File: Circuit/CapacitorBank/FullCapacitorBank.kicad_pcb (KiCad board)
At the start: 2 copper layers, 142.2 x 101.6 mm, 48 parts, among them J1 AC Power In, J2 Output+, J3 Output-, J4 To Voltage Sensing, Q1 BT138-800, Q2 BT138-800, SW1 SW_Push, T1 6:75+75, U1 PC817, U2 PC817

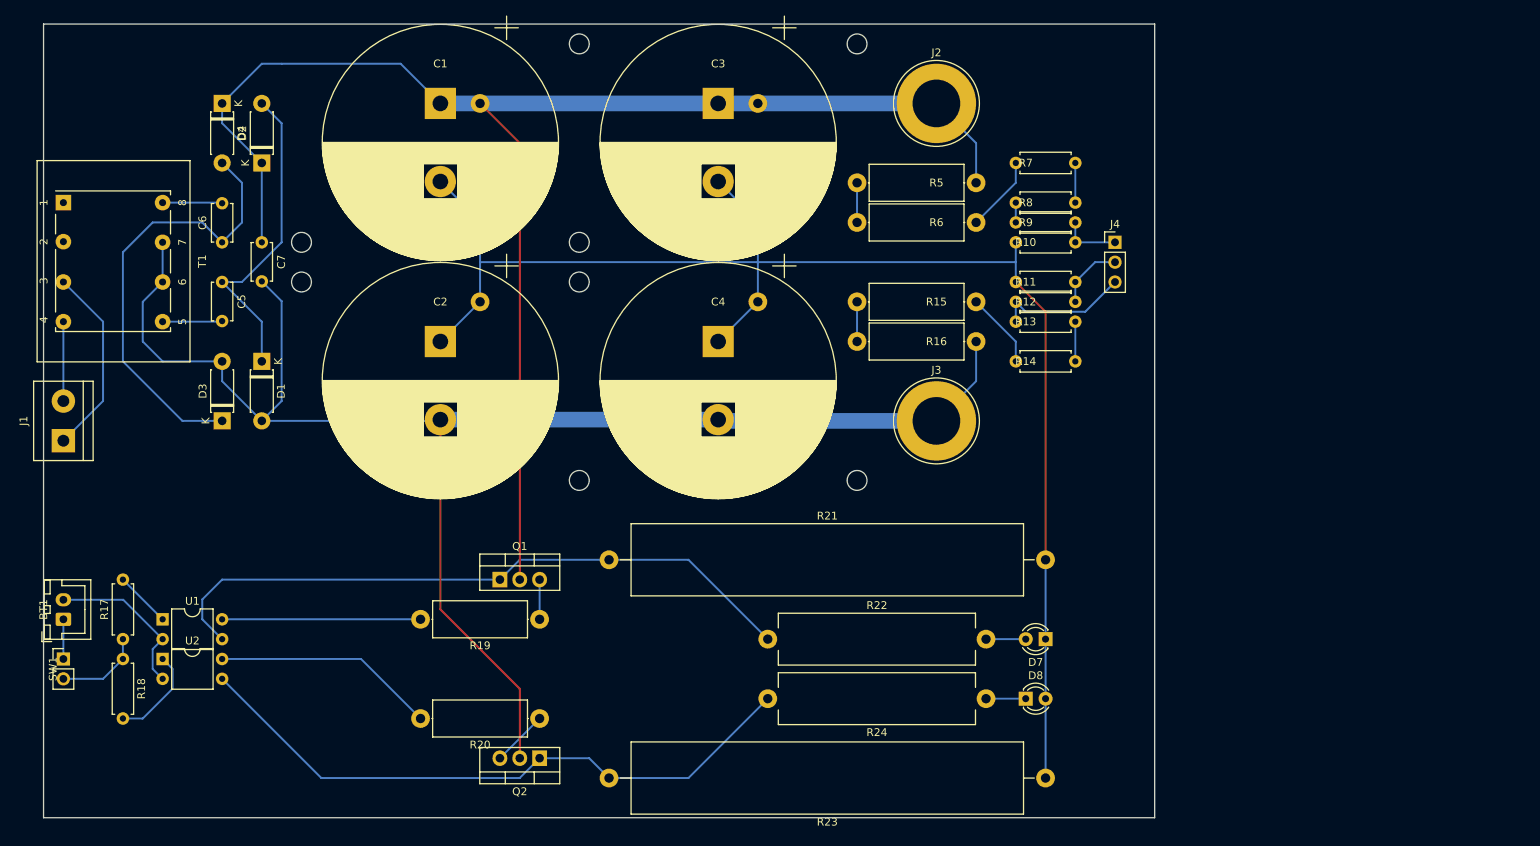
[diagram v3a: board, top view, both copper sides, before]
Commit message: [Circuit] Adjust footprint of customized components and optimize the PCB design
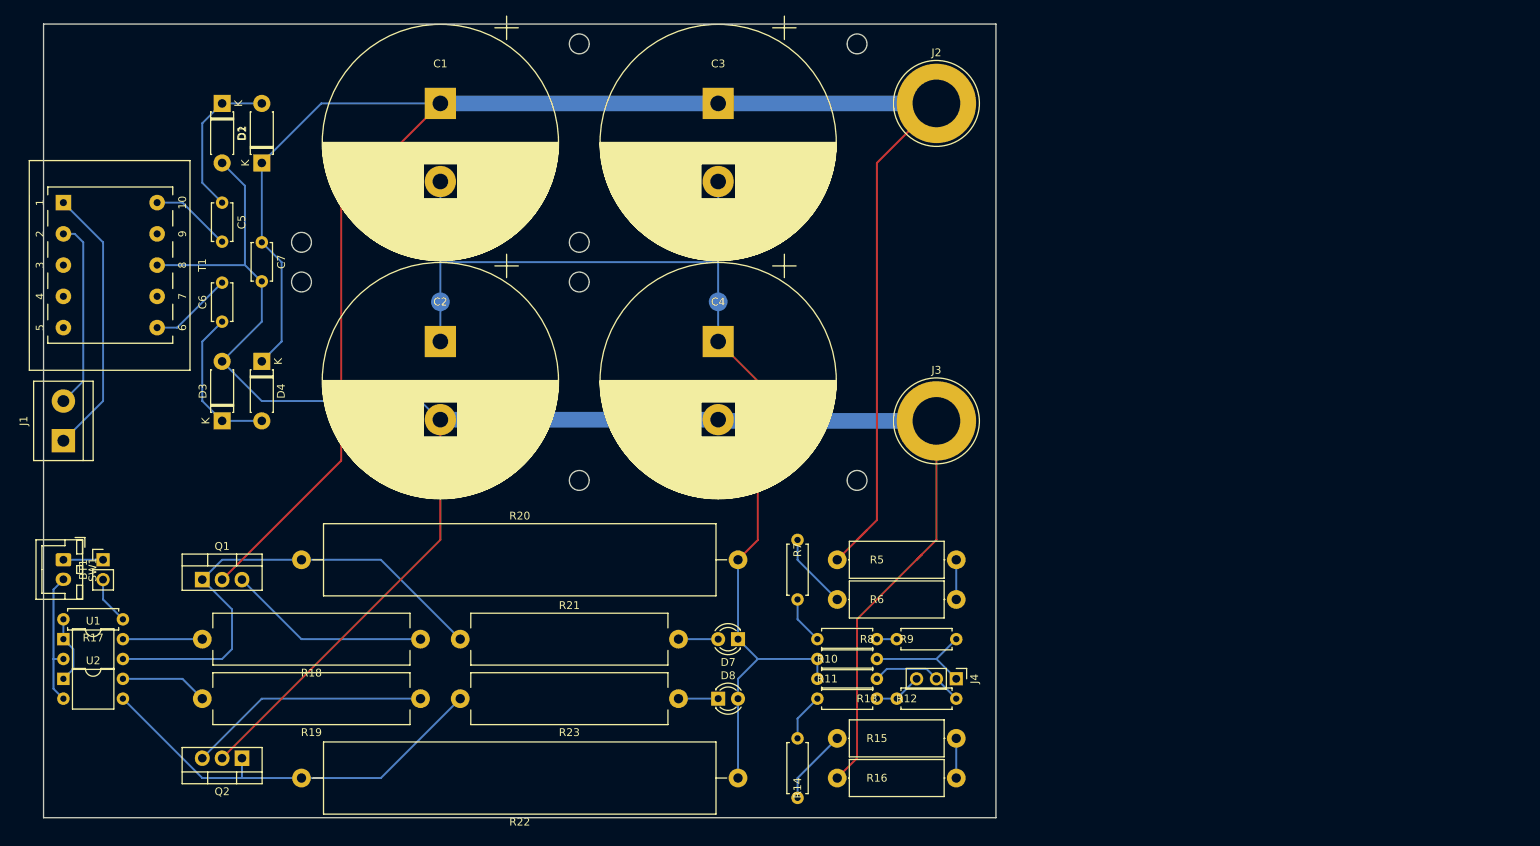
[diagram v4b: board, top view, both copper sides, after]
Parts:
- removed the R18 at (55.9, 114.3)
- R17: value 1K -> 510
- R18: renamed from R19; value 1M/1W -> 43K/5W; footprint Resistor_THT:R_Axial_DIN0414_L11.9mm_D4.5mm_P15.24mm_Horizontal -> Resistor_THT:R_Axial_Power_L25.0mm_W6.4mm_P27.94mm
- R19: renamed from R20; value 1M/1W -> 43K/5W; footprint Resistor_THT:R_Axial_DIN0414_L11.9mm_D4.5mm_P15.24mm_Horizontal -> Resistor_THT:R_Axial_Power_L25.0mm_W6.4mm_P27.94mm
- T1: footprint Power:Transformer_Generic_EE25_8Pin -> Power:Transformer_Generic_EE25_10Pin
- moved R8 64.9 mm to (144.8, 111.8), turned to 0 degrees
- moved R14 59.9 mm to (142.2, 124.5), turned to 270 degrees
- moved J4 59.5 mm to (162.6, 116.8), turned to 270 degrees
- moved R10 59.1 mm to (152.4, 114.3)
- moved R15 58.6 mm to (147.3, 124.5), turned to 0 degrees
- moved R16 57.3 mm to (162.6, 129.5), turned to 180 degrees
- moved R11 56.8 mm to (144.8, 116.8)
- moved R7 55.8 mm to (142.2, 99.1), turned to 270 degrees
- moved R9 55.5 mm to (154.9, 111.8)
- moved R12 53.0 mm to (162.6, 119.4)
- moved R13 51.4 mm to (152.4, 119.4), turned to 180 degrees
- moved R5 51.4 mm to (147.3, 101.6), turned to 0 degrees
- moved R6 49.9 mm to (162.6, 106.7), turned to 180 degrees
- moved D7 39.4 mm to (134.6, 111.8)
- moved R20 39.4 mm to (78.7, 101.6)
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- renumbered R21 to R20, R22 to R21, R23 to R22, R24 to R23
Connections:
- T1 pad 1: (no net) -> /ACPowerIn+
- T1 pad 2: (no net) -> /ACPowerIn-
- T1 pad 3: /ACPowerIn+ -> (no net)
- T1 pad 4: /ACPowerIn- -> (no net)
- T1 pad 5: Net-(C5-Pad2) -> (no net)
- T1 pad 6: /PowerOut- -> Net-(C6-Pad2)
- T1 pad 7: /PowerOut- -> (no net)
- T1 pad 8: Net-(C6-Pad2) -> /PowerOut-
- U2 pad 1: Net-(R18-Pad2) (its old number) -> Net-(R17-Pad2)
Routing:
- net /PowerOut+: track 190.9 -> 255.0 mm
- net /PowerOut-: track 200.7 -> 242.3 mm
- net Net-(C1-Pad2): track 188.2 -> 147.8 mm
- net Net-(C6-Pad1): track 57.4 -> 19.9 mm
- net Net-(Q2-Pad1): track 81.4 -> 54.1 mm
- net Net-(Q2-Pad3): track 7.18 -> 31.1 mm
- net Net-(Q1-Pad1): track 84.8 -> 63.2 mm
- net Net-(C5-Pad1): track 40.8 -> 19.9 mm
- net Net-(Q1-Pad3): track 5.08 -> 26.0 mm
- net Net-(R19-Pad2): track 28.6 -> 11.2 mm
- net Net-(R18-Pad2): track 25.4 -> 10.2 mm
- net /ACPowerIn-: track 10.2 -> 24.4 mm
- net Net-(R18-Pad2) (its old number): track 12.3 -> 0.00 mm
- net /Sensor0V: track 17.3 -> 6.13 mm
- net /ACPowerIn+: track 24.5 -> 34.8 mm
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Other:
- board size 142.2 x 101.6 mm -> 121.9 x 101.6 mm

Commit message: [Circuit] Add screw holes to PCBs
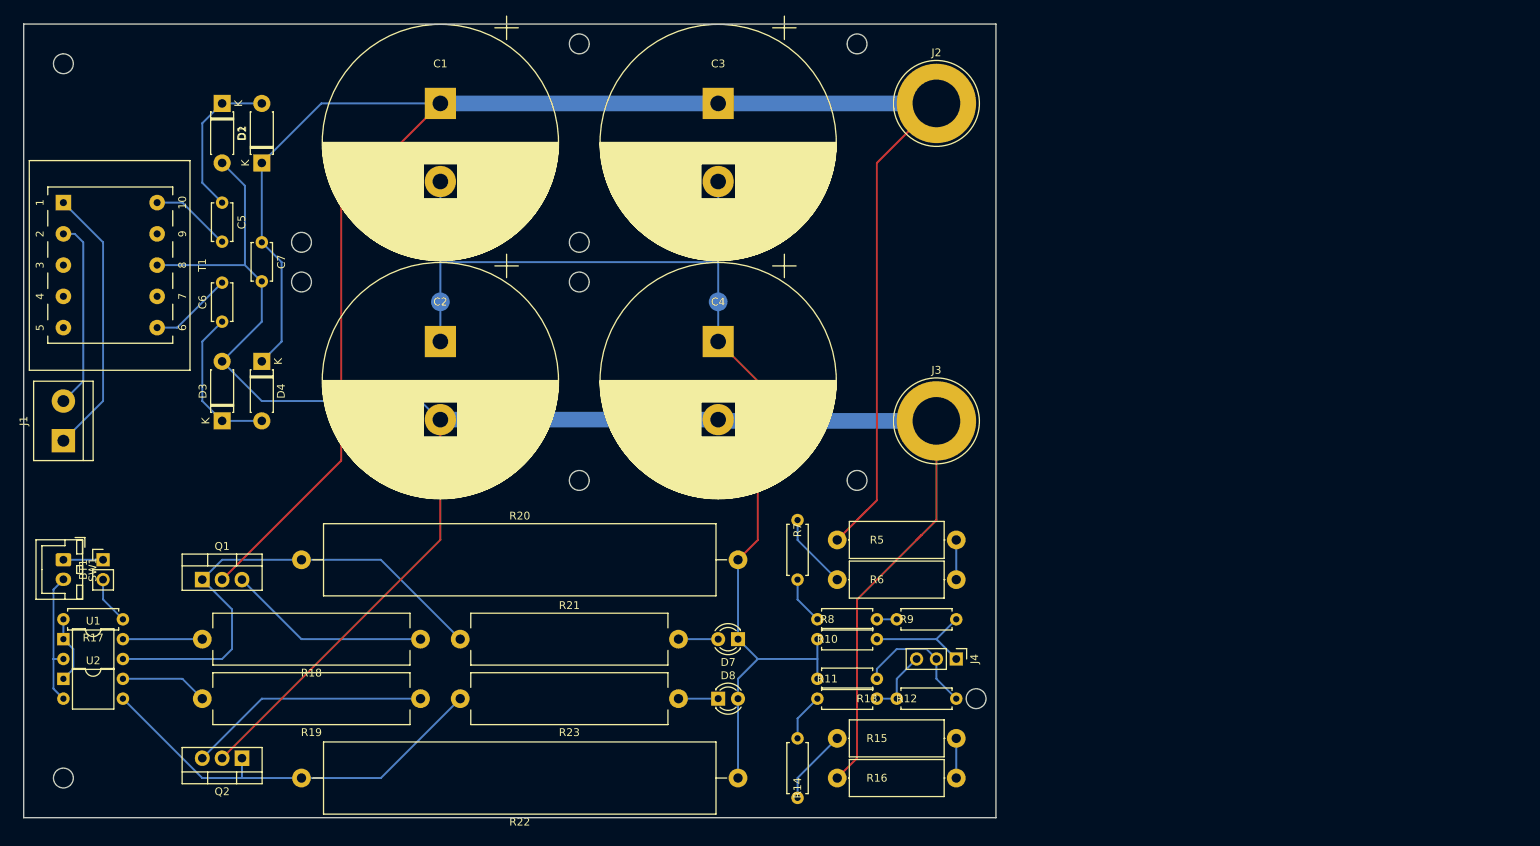
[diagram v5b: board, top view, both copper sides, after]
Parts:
- moved J4 2.54 mm to (162.6, 114.3)
- moved R6 2.54 mm to (162.6, 104.1)
- moved R7 2.54 mm to (142.2, 96.5)
- moved R8 2.54 mm to (144.8, 109.2)
- moved R9 2.54 mm to (154.9, 109.2)
- moved R10 2.54 mm to (152.4, 111.8)
- moved R5 2.54 mm to (147.3, 99.1)
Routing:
- net /Sensor3V: track 12.3 -> 16.6 mm
- net /PowerOut+: track 255.0 -> 252.5 mm
- net /Sensor0V: track 6.13 -> 8.67 mm
- net Net-(C1-Pad2): track 147.8 -> 150.4 mm
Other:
- board size 121.9 x 101.6 mm -> 124.5 x 101.6 mm

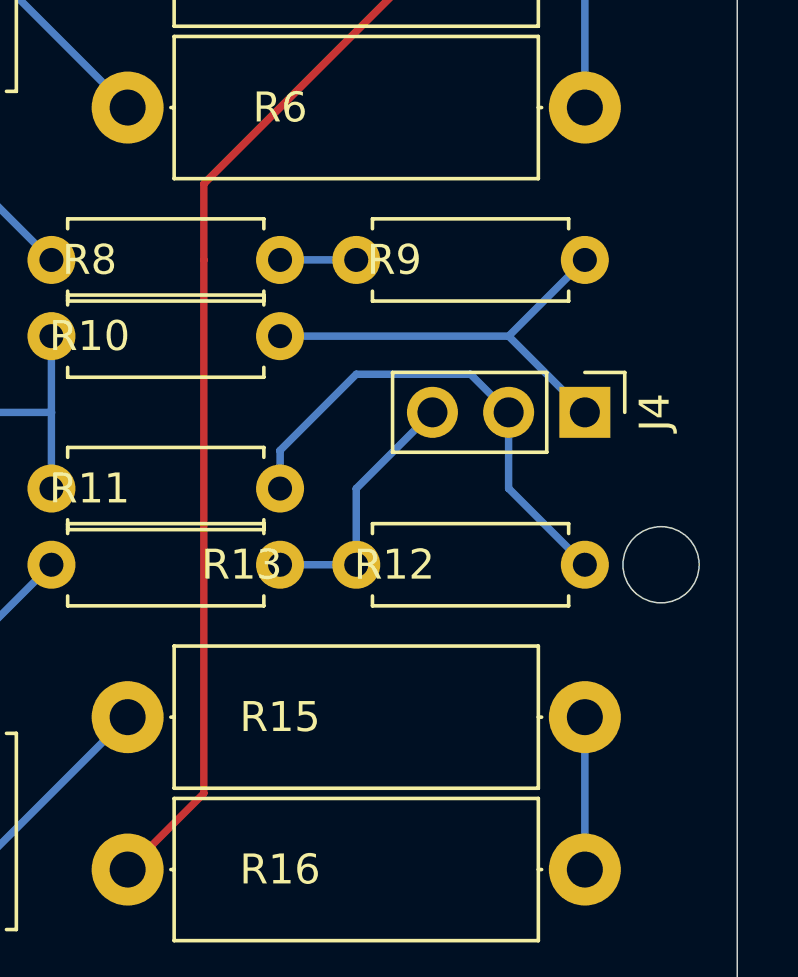
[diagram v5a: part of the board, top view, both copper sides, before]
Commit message: [Circuit] One channel voltage sensing and control modules
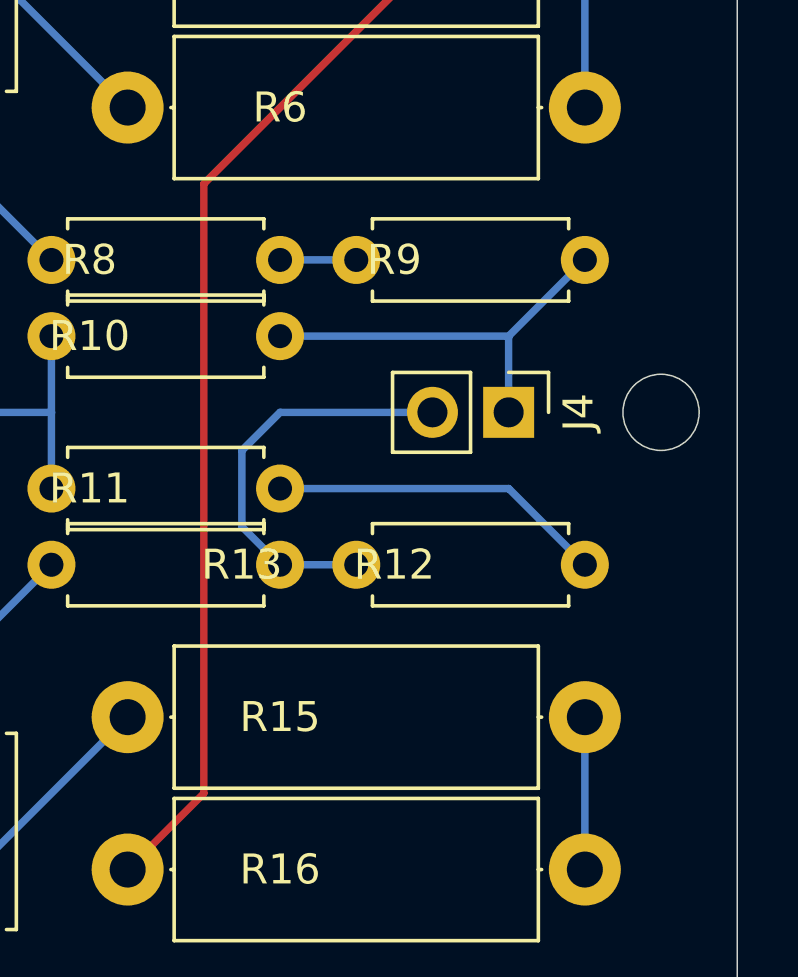
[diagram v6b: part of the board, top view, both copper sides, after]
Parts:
- J4: footprint Connector_PinHeader_2.54mm:PinHeader_1x03_P2.54mm_Vertical -> Connector_PinHeader_2.54mm:PinHeader_1x02_P2.54mm_Vertical
- R15, R16, R5, R6: value 1M -> 1M/1W
- moved J4 2.54 mm to (160.0, 114.3)
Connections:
- J4 pad 2: /Sensor3V -> /Sensor0V
- R11 pad 2: /Sensor3V -> Net-(R11-Pad2)
- R12 pad 1: /Sensor3V -> Net-(R11-Pad2)
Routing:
- net /Sensor3V: track 16.6 -> 0.00 mm
- net Net-(R11-Pad2): track 0.00 -> 11.2 mm
- net /Sensor0V: track 8.67 -> 13.8 mm
- net /Sensor9V: track 14.8 -> 13.8 mm
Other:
- outline, holes or cut-outs redrawn

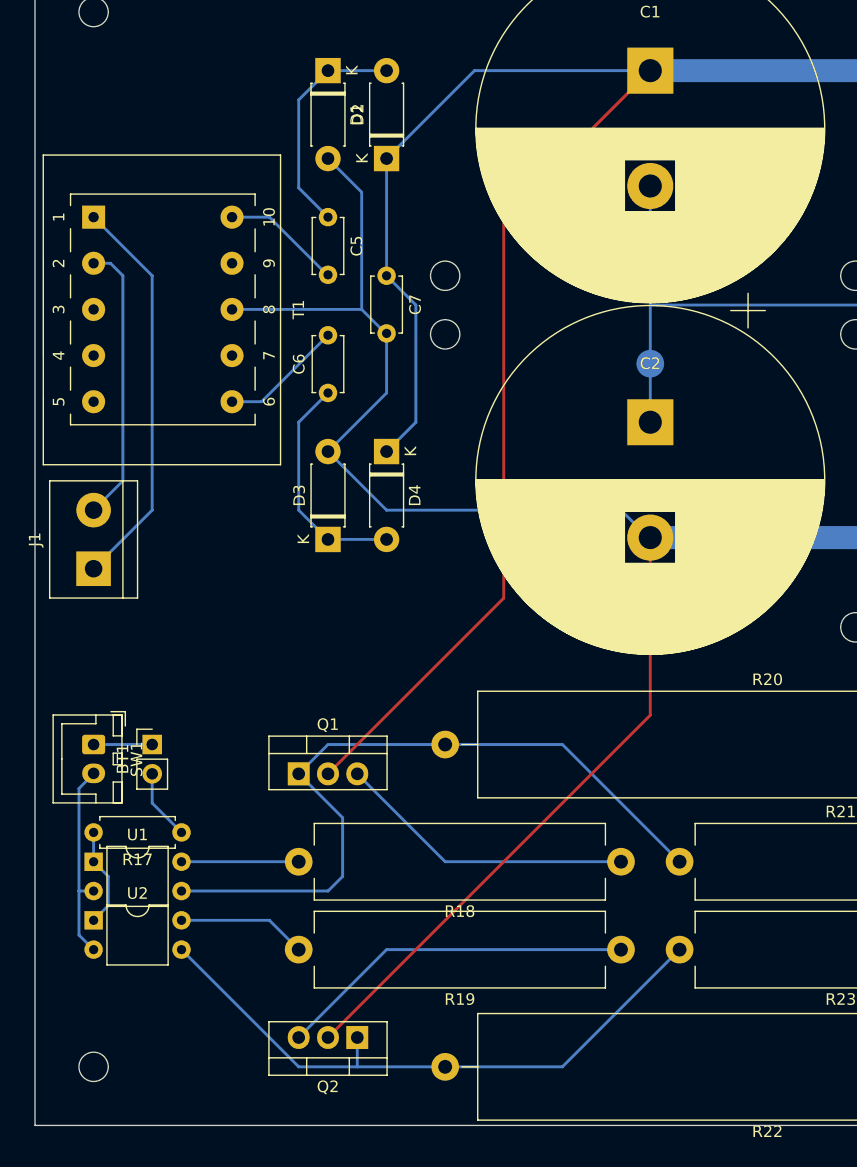
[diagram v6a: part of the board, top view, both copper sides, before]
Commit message: [Circuit] Add a discharge signal to capacitor bank
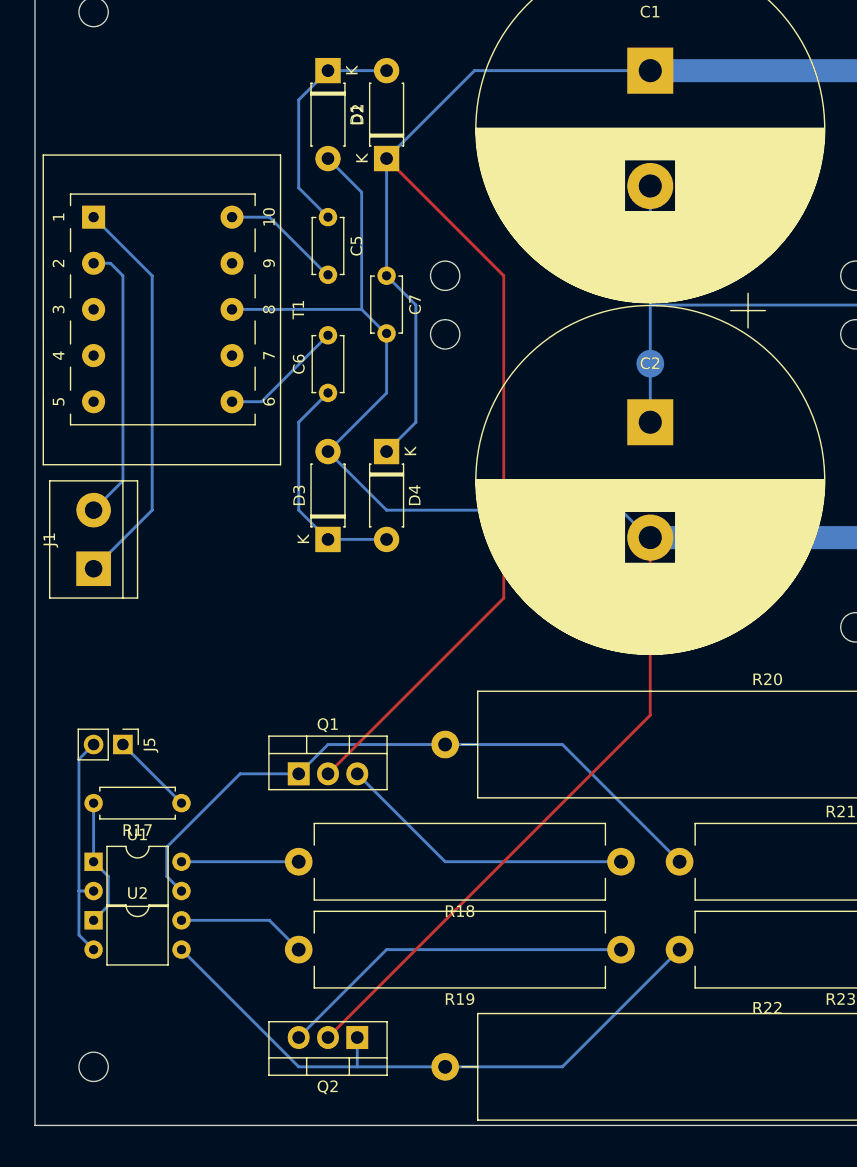
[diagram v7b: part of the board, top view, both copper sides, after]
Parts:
- removed BT1: 12V Battery, Connector_JST:JST_XH_B2B-XH-A_1x02_P2.50mm_Vertical
- removed SW1: SW_Push, Connector_PinHeader_2.54mm:PinHeader_1x02_P2.54mm_Vertical
- added J5: To Voltage Sensing, Connector_PinHeader_2.54mm:PinHeader_1x02_P2.54mm_Vertical, F.Cu at (50.8, 101.6)
- moved R17 2.54 mm to (55.9, 106.7)
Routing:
- net /PowerOut+: track 252.5 -> 243.8 mm
- net Net-(Q1-Pad1): track 63.2 -> 56.7 mm
- net Net-(BT1-Pad1): track 5.08 -> 0.00 mm
- net Net-(R17-Pad2): track 8.67 -> 11.2 mm
- net Net-(J5-Pad2): track 17.6 -> 20.1 mm
- net Net-(J5-Pad1): track 6.13 -> 7.18 mm
